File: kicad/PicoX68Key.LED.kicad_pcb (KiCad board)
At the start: 2 copper layers, 33.9 x 36.5 mm, 22 parts, among them J1 LED_BOARD, U1 74HCT595, U2 74HCT595

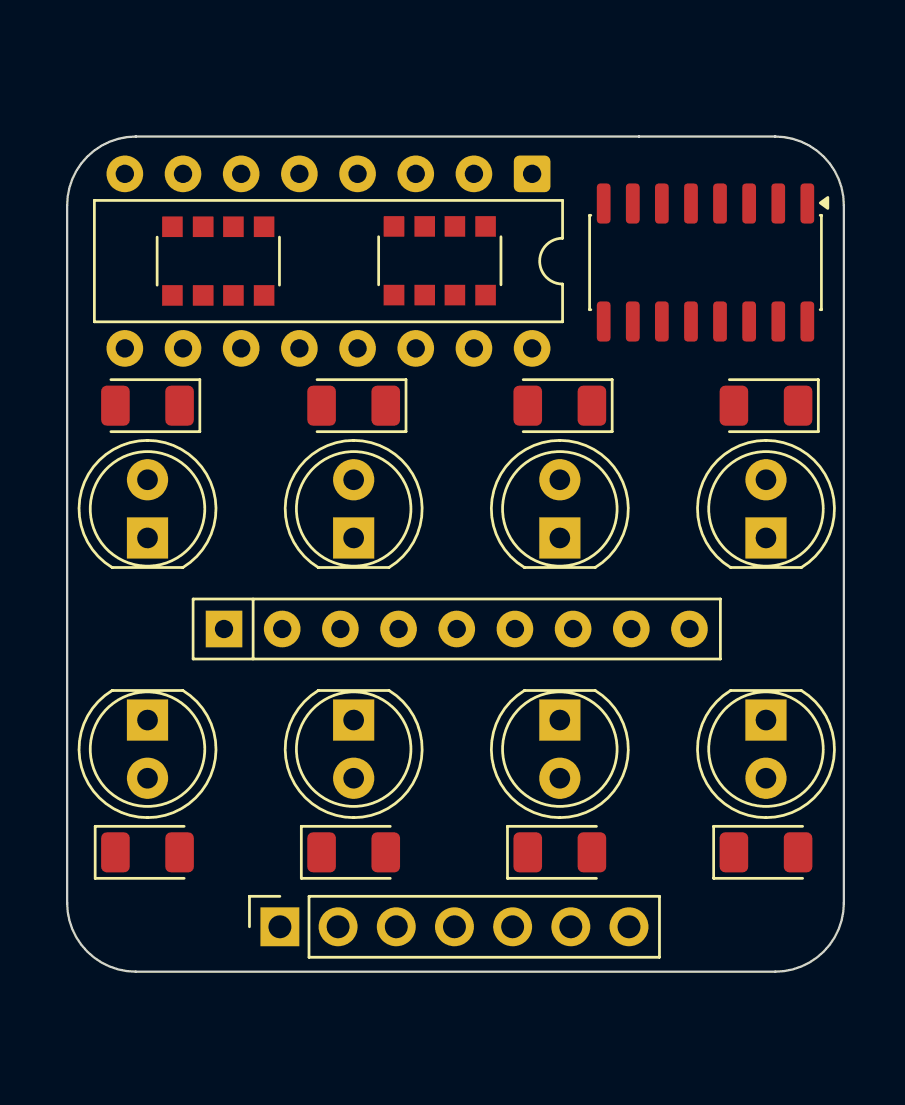
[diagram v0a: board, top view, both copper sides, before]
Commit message: Create LED board and tweak designs
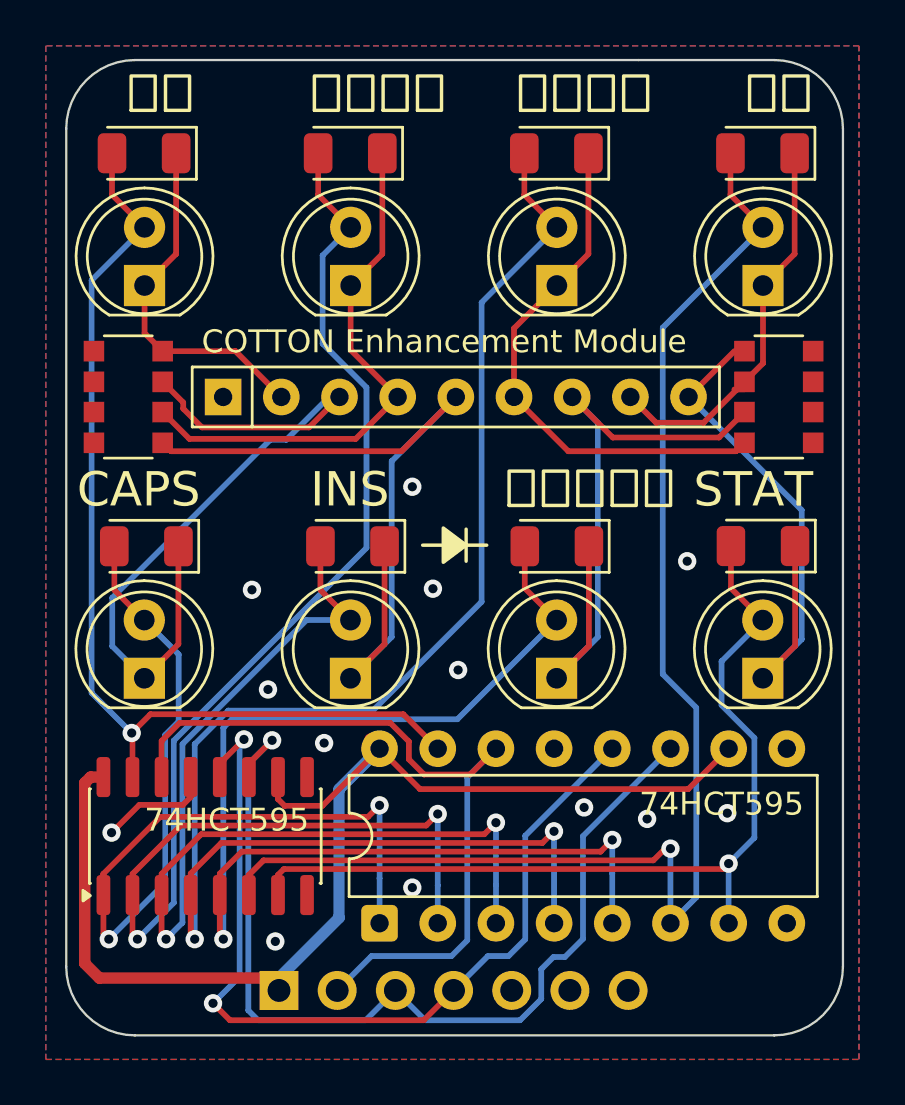
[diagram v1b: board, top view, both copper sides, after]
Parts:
- added G***: LOGO, Library:X68000_Logo_Small, B.Cu at (83.7, 75.3)
- J1: moved to B.Cu
- moved U1 33.4 mm to (80.6, 78.8), turned to 90 degrees
- moved U2 33.2 mm to (73.0, 75.0), turned to 90 degrees
- moved RN3 15.9 mm to (98.0, 55.8), turned to 180 degrees
- moved D16 13.4 mm to (97.3, 62.3), turned to 180 degrees
- moved D12 13.4 mm to (88.3, 62.4), turned to 180 degrees
- moved D11 13.4 mm to (70.4, 62.4), turned to 180 degrees
- moved D15 13.4 mm to (79.4, 62.4), turned to 180 degrees
- moved D10 11.0 mm to (88.3, 45.2)
- moved D13 11.0 mm to (79.3, 45.2)
- moved D14 11.0 mm to (97.3, 45.2)
- moved D9 11.0 mm to (70.3, 45.2)
- moved D1 11.0 mm to (70.3, 51.0)
- moved D3 11.0 mm to (79.3, 51.0)
- moved D5 11.0 mm to (88.3, 51.0)
- moved D7 11.0 mm to (97.3, 51.0)
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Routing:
- net /QE: track 0.00 -> 68.7 mm, vias 0 -> 2
- net /QC: track 0.00 -> 62.5 mm, vias 0 -> 2
- net /QG: track 0.00 -> 60.1 mm, vias 0 -> 1
- net +5V: track 0.00 -> 54.0 mm
- net /QF: track 0.00 -> 53.8 mm, vias 0 -> 2
- net /QD: track 0.00 -> 45.0 mm, vias 0 -> 2
- net /QA: track 0.00 -> 43.8 mm, vias 0 -> 1
- net /SCL: track 0.00 -> 42.2 mm, vias 0 -> 1
- net /QB: track 0.00 -> 41.4 mm, vias 0 -> 2
- net /QH: track 0.00 -> 39.6 mm, vias 0 -> 1
- net /CS: track 0.00 -> 39.5 mm, vias 0 -> 2
- net Net-(D15-K): track 0.00 -> 34.5 mm
- net /MOSI: track 0.00 -> 33.8 mm
- net Net-(D11-K): track 0.00 -> 33.3 mm
- net Net-(D12-K): track 0.00 -> 28.5 mm
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- added copper zone on B.Cu, net GND
- added copper zone on F.Cu, net GND
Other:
- board size 33.9 x 36.5 mm -> 33.9 x 42.6 mm
- board text added: "CAPS"
- board text added: "COTTON Enhancement Module"
- board text added: "INS"
- board text added: "STAT"
- board text added: "THIS PAGE INTENTIONALLY LEFT BLANK"
- board text added: "かな"
- board text added: "ひらがな"
- board text added: "コード入力"
- board text added: "ローマ字"
- board text added: "全角"

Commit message: Fixed B2B interconnect clearance
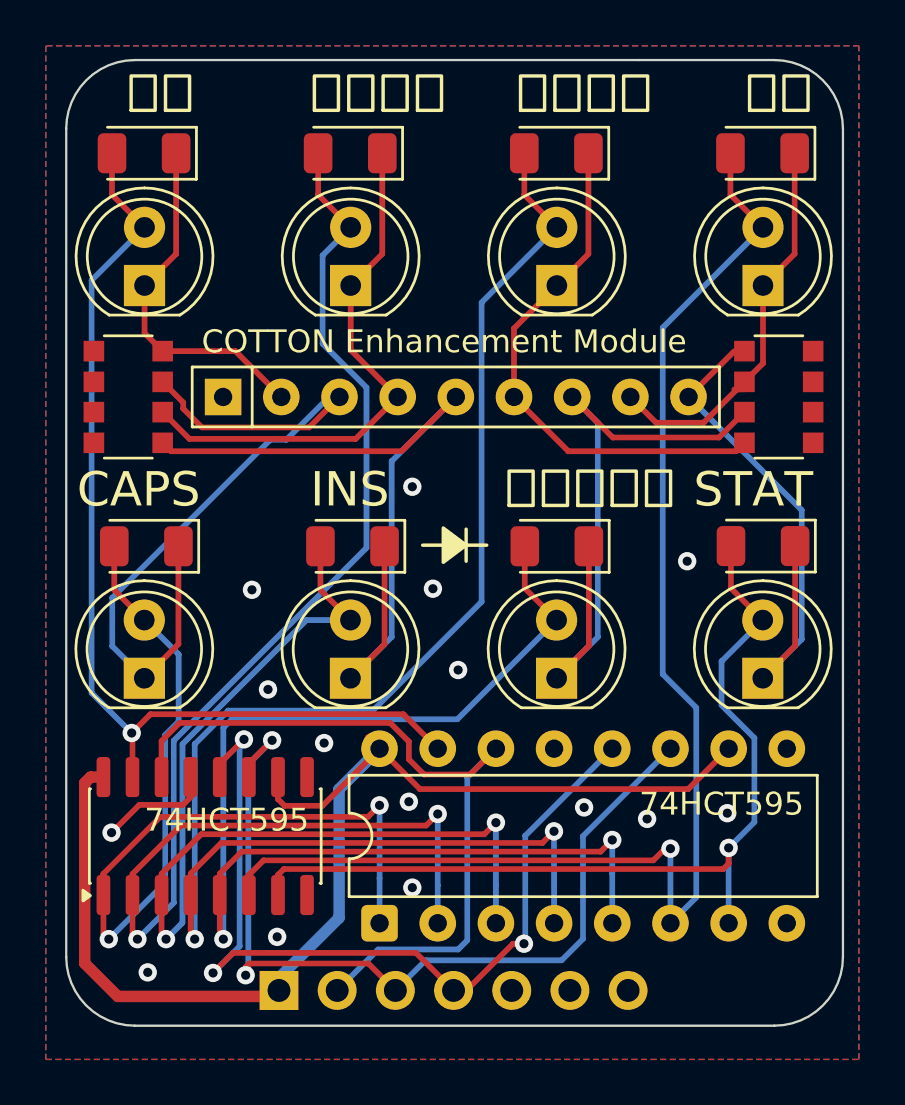
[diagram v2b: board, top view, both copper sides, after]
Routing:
- net /SCL: track 42.2 -> 39.2 mm, vias 1 -> 2
- net /CS: track 39.5 -> 38.4 mm, vias 2 -> 3
- net /QH: track 39.6 -> 40.3 mm
- net GND: track 4.97 -> 5.15 mm, vias 13 -> 15
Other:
- board size 33.9 x 42.6 mm -> 33.9 x 42.2 mm

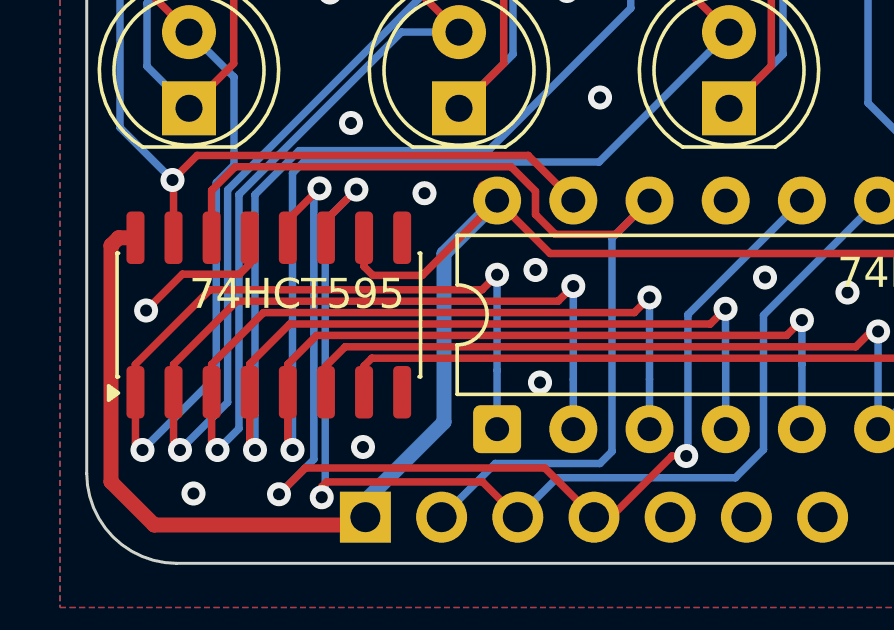
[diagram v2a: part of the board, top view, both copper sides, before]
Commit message: Fix ground plane
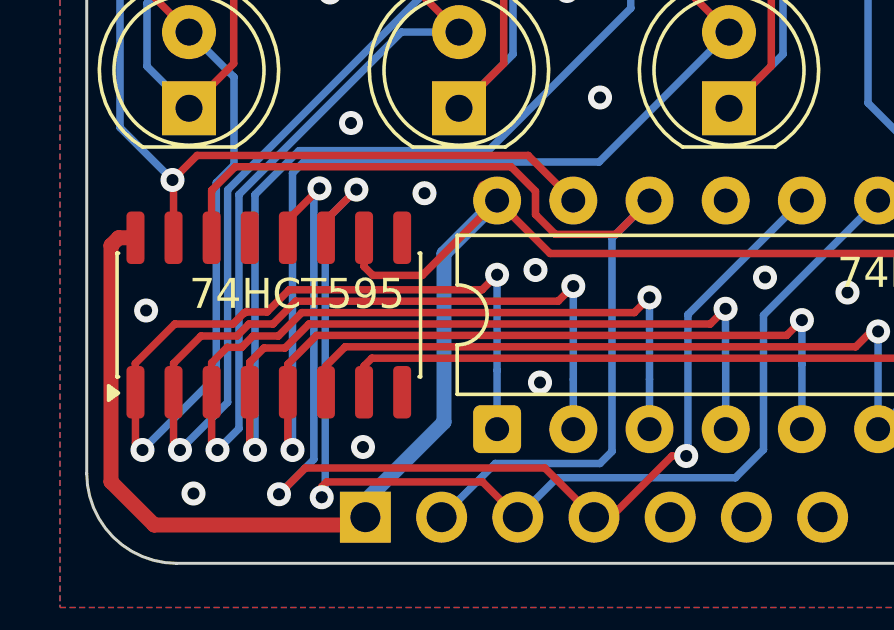
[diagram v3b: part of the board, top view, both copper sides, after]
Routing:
- net GND: track 5.15 -> 0.18 mm
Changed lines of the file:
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@@
+	)
+	(segment
+		(start 72.178 74.922)
+		(end 72.143427 74.922)
+		(width 0.25)
+		(layer "F.Cu")
+		(net 4)
+	)
+	(segment
+		(start 68.515 79.265)
+		(end 68.75 79.5)
+		(width 0.25)
+		(layer "F.Cu")
+		(net 4)
 	)
 	(segment
@@
 	)
 	(segment
-		(start 71 74.16)
-		(end 68.51 76.65)
-		(width 0.25)
-		(layer "F.Cu")
-		(net 4)
-	)
-	(segment
-		(start 68.515 79.265)
-		(end 68.75 79.5)
-		(width 0.25)
-		(layer "F.Cu")
-		(net 4)
-	)
-	(segment
-		(start 80.068 74.16)
-		(end 71 74.16)
+		(start 72.2 74.9)
+		(end 72.178 74.922)
 		(width 0.25)
 		(layer "F.Cu")
@@
 	)
 	(segment
+		(start 71.765428 75.3)
+		(end 69.825 75.3)
+		(width 0.25)
+		(layer "F.Cu")
+		(net 4)
+	)
+	(segment
 		(start 68.99 64.26)
 		(end 70.3 65.57)
@@
 	)
 	(segment
-		(start 68.51 76.65)
+		(start 69.825 75.3)
+		(end 68.51 76.615)
+		(width 0.25)
+		(layer "F.Cu")
+		(net 4)
+	)
+	(segment
+		(start 73.64 74.16)
+		(end 72.9 74.9)
+		(width 0.25)
+		(layer "F.Cu")
+		(net 4)
+	)
+	(segment
+		(start 68.51 76.615)
 		(end 68.51 77.575)
+		(width 0.25)
+		(layer "F.Cu")
+		(net 4)
+	)
+	(segment
+		(start 80.068 74.16)
+		(end 73.64 74.16)
 		(width 0.25)
 		(layer "F.Cu")
@@
 		(net 4)
 	)
+	(segment
+		(start 72.9 74.9)
+		(end 72.2 74.9)
+		(width 0.25)
+		(layer "F.Cu")
+		(net 4)
+	)
+	(segment
+		(start 72.143427 74.922)
+		(end 71.765428 75.3)
+		(width 0.25)
+		(layer "F.Cu")
+		(net 4)
+	)
 	(via
 		(at 80.57 73.658)
@@
 	)
 	(segment
-		(start 69.785 76.65)
+		(start 69.785 76.615)
 		(end 69.785 77.575)
 		(width 0.25)
@@
 	)
 	(segment
-		(start 71.895 74.54)
-		(end 69.785 76.65)
+		(start 71.9 75.7)
+		(end 70.7 75.7)
+		(width 0.25)
+		(layer "F.Cu")
+		(net 5)
+	)
+	(segment
+		(start 73.1 75.3)
+		(end 72.3 75.3)
+		(width 0.25)
+		(layer "F.Cu")
+		(net 5)
+	)
+	(segment
+		(start 77.89 45.19)
+		(end 77.89 47.005)
+		(width 0.25)
+		(layer "F.Cu")
+		(net 5)
+	)
+	(segment
+		(start 73.86 74.54)
+		(end 73.1 75.3)
+		(width 0.25)
+		(layer "F.Cu")
+		(net 5)
+	)
+	(segment
+		(start 82.606 74.54)
+		(end 73.86 74.54)
+		(width 0.25)
+		(layer "F.Cu")
+		(net 5)
+	)
+	(segment
+		(start 72.3 75.3)
+		(end 71.9 75.7)
+		(width 0.25)
+		(layer "F.Cu")
+		(net 5)
+	)
+	(segment
+		(start 70.7 75.7)
+		(end 69.785 76.615)
 		(width 0.25)
 		(layer "F.Cu")
@@
 		(net 5)
 	)
-	(segment
-		(start 77.89 45.19)
-		(end 77.89 47.005)
-		(width 0.25)
-		(layer "F.Cu")
-		(net 5)
-	)
-	(segment
-		(start 82.606 74.54)
-		(end 71.895 74.54)
-		(width 0.25)
-		(layer "F.Cu")
-		(net 5)
-	)
 	(via
 		(at 70 79.5)
@@
 	)
 	(segment
+		(start 71.055 76.595)
+		(end 71.055 77.575)
+		(width 0.25)
+		(layer "F.Cu")
+		(net 8)
+	)
+	(segment
+		(start 74.06 74.92)
+		(end 73.28 75.7)
+		(width 0.25)
+		(layer "F.Cu")
+		(net 8)
+	)
+	(segment
 		(start 85.65 74.414)
 		(end 85.144 74.92)
@@
 	)
 	(segment
-		(start 71.055 76.65)
-		(end 71.055 77.575)
-		(width 0.25)
-		(layer "F.Cu")
-		(net 8)
-	)
-	(segment
-		(start 72.785 74.92)
-		(end 71.055 76.65)
+		(start 72.434572 75.7)
+		(end 72.056572 76.078)
+		(width 0.25)
+		(layer "F.Cu")
+		(net 8)
+	)
+	(segment
+		(start 72.056572 76.078)
+		(end 71.572 76.078)
+		(width 0.25)
+		(layer "F.Cu")
+		(net 8)
+	)
+	(segment
+		(start 71.572 76.078)
+		(end 71.055 76.595)
 		(width 0.25)
 		(layer "F.Cu")
@@
 	)
 	(segment
-		(start 85.144 74.92)
-		(end 72.785 74.92)
-		(width 0.25)
-		(layer "F.Cu")
-		(net 8)
-	)
-	(segment
 		(start 77.99 62.35)
 		(end 77.99 64.26)
@@
 	)
 	(segment
+		(start 85.144 74.92)
+		(end 74.06 74.92)
+		(width 0.25)
+		(layer "F.Cu")
+		(net 8)
+	)
+	(segment
 		(start 71.055 79.305)
 		(end 71.25 79.5)
@@
 		(net 8)
 	)
+	(segment
+		(start 73.28 75.7)
+		(end 72.434572 75.7)
+		(width 0.25)
+		(layer "F.Cu")
+		(net 8)
+	)
 	(via
 		(at 71.25 79.5)
@@
 	)
 	(segment
+		(start 72.325 76.575)
+		(end 72.325 77.575)
+		(width 0.25)
+		(layer "F.Cu")
+		(net 9)
+	)
+	(segment
+		(start 74.3 75.3)
+		(end 73.5 76.1)
+		(width 0.25)
+		(layer "F.Cu")
+		(net 9)
+	)
+	(segment
 		(start 87.677 75.3)
-		(end 73.66 75.3)
-		(width 0.25)
-		(layer "F.Cu")
-		(net 9)
-	)
-	(segment
-		(start 73.66 75.3)
-		(end 72.325 76.635)
+		(end 74.3 75.3)
 		(width 0.25)
 		(layer "F.Cu")
@@
 	)
 	(segment
+		(start 72.8 76.1)
+		(end 72.325 76.575)
+		(width 0.25)
+		(layer "F.Cu")
+		(net 9)
+	)
+	(segment
+		(start 73.5 76.1)
+		(end 72.8 76.1)
+		(width 0.25)
+		(layer "F.Cu")
+		(net 9)
+	)
+	(segment
 		(start 86.89 47.005)
 		(end 88.31 48.425)
-		(width 0.25)
-		(layer "F.Cu")
-		(net 9)
-	)
-	(segment
-		(start 72.325 76.635)
-		(end 72.325 77.575)
 		(width 0.25)
 		(layer "F.Cu")
@@
 	)
 	(segment
-		(start 72.325 72.425)
-		(end 72.325 73.299999)
-		(width 0.25)
-		(layer "F.Cu")
-		(net 23)
-	)
-	(segment
 		(start 82.128 77.122)
 		(end 82 77.25)
-		(width 0.25)
-		(layer "F.Cu")
-		(net 23)
-	)
-	(segment
-		(start 72.325 73.299999)
-		(end 71.984999 73.64)
-		(width 0.25)
-		(layer "F.Cu")
-		(net 23)
-	)
-	(segment
-		(start 71.984999 73.64)
-		(end 70.08 73.64)
-		(width 0.25)
-		(layer "F.Cu")
-		(net 23)
-	)
-	(segment
-		(start 70.08 73.64)
-		(end 68.87 74.85)
 		(width 0.25)
 		(layer "F.Cu")
@@
 			)
 		)
-	)
-	(zone
-		(net 0)
-		(net_name "")
-		(layer "F.Cu")
-		(hatch edge 0.5)
-		(connect_pads
-			(clearance 0)
-		)
-		(min_thickness 0.25)
-		(filled_areas_thickness no)
-		(keepout
-			(tracks allowed)
-			(vias allowed)
-			(pads allowed)
-			(copperpour not_allowed)
-			(footprints allowed)
-		)
-		(placement
-			(enabled no)
-			(sheetname "/")
-		)
-		(fill
-			(thermal_gap 0.5)
-			(thermal_bridge_width 0.5)
-		)
-		(polygon
-			(pts
-				(xy 71.25 70.25) (xy 74 70.25) (xy 74 71.75) (xy 71.25 71.75)
-			)
-		)

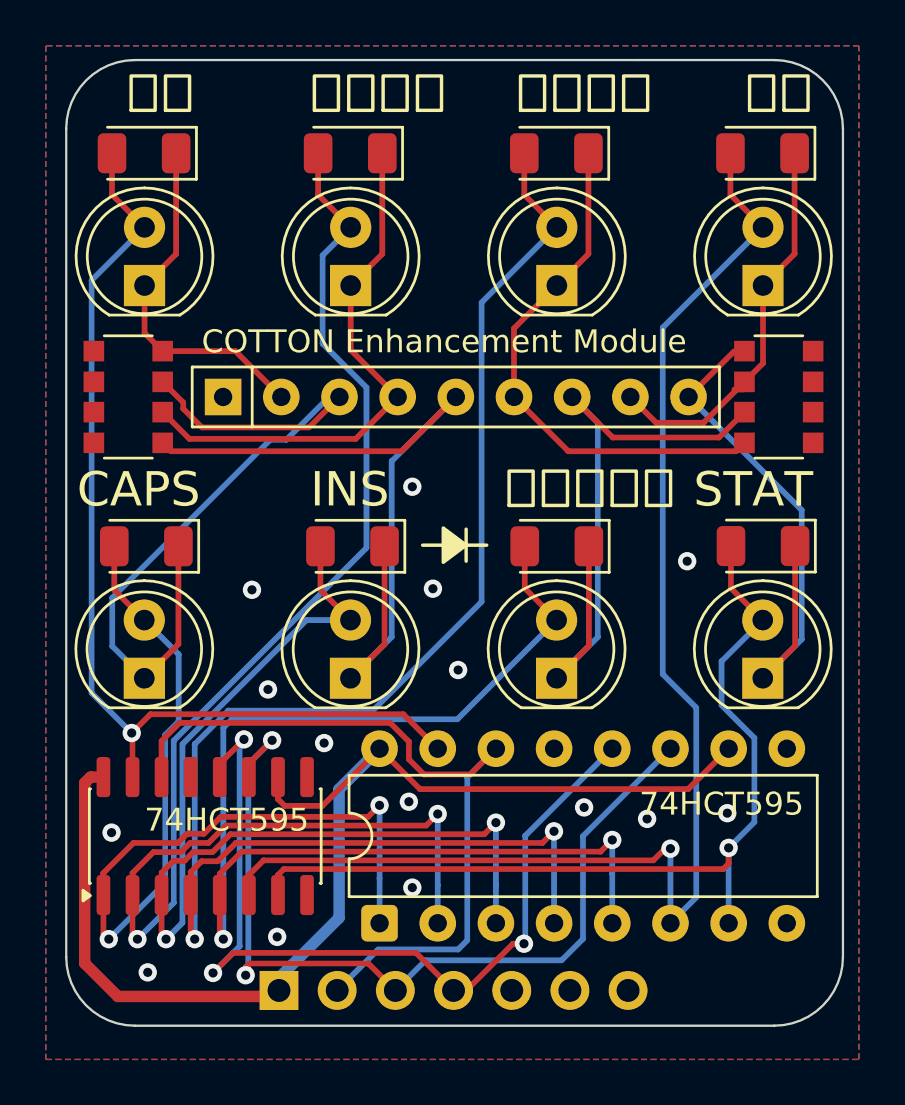
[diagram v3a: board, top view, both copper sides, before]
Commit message: Add PWM functionality to set LED brightness
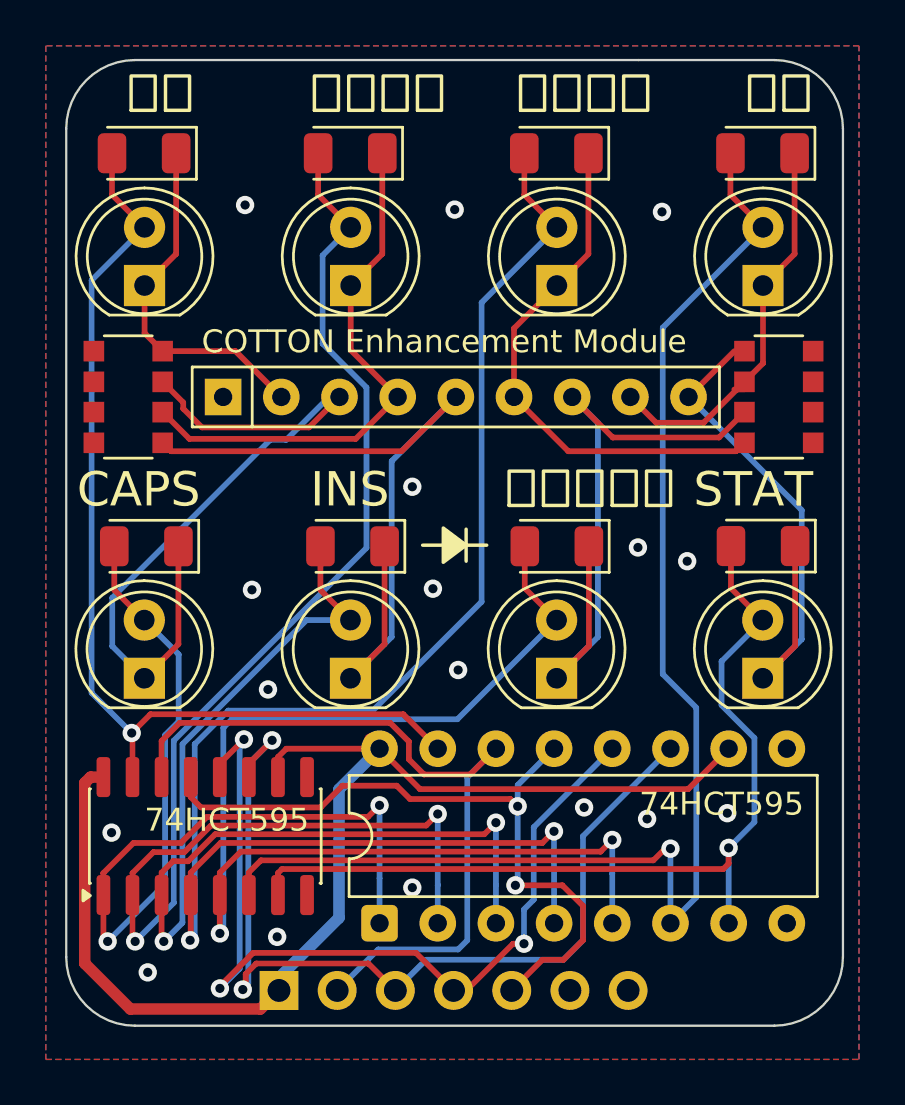
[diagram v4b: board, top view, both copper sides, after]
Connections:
- J1 pad 5: unconnected-(J1-Pin_5-Pad5) -> /OE
- U1 pad 13: GND -> /OE
- U2 pad 13: GND -> /OE
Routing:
- net /OE: track 0.00 -> 31.6 mm, vias 0 -> 2
- net /SCL: track 39.2 -> 40.4 mm
- net +5V: track 54.2 -> 53.6 mm
- net /CS: track 38.4 -> 39.0 mm
- net GND: vias 15 -> 17
